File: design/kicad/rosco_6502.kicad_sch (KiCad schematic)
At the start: 54 parts, among them IC1 W65C02SxP, IC2 ATF22V10C-7PX, IC3 XR68C681CJTR-F, IC4 NE555P, IC5 ATF22V10C-7PX, J1 UART_A, J2 UART_B, J3 Conn_01x06, J4 Conn_01x01_Male, J5 Conn_02x18_Odd_Even, J6 Conn_01x02_Male, Q1 3.6864MHz, U1 AS6C4008-55PCN, U2 AS6C62256-55PCN, U3 AT28C64B-15PU, U4 74HCT174, X1 14MHz

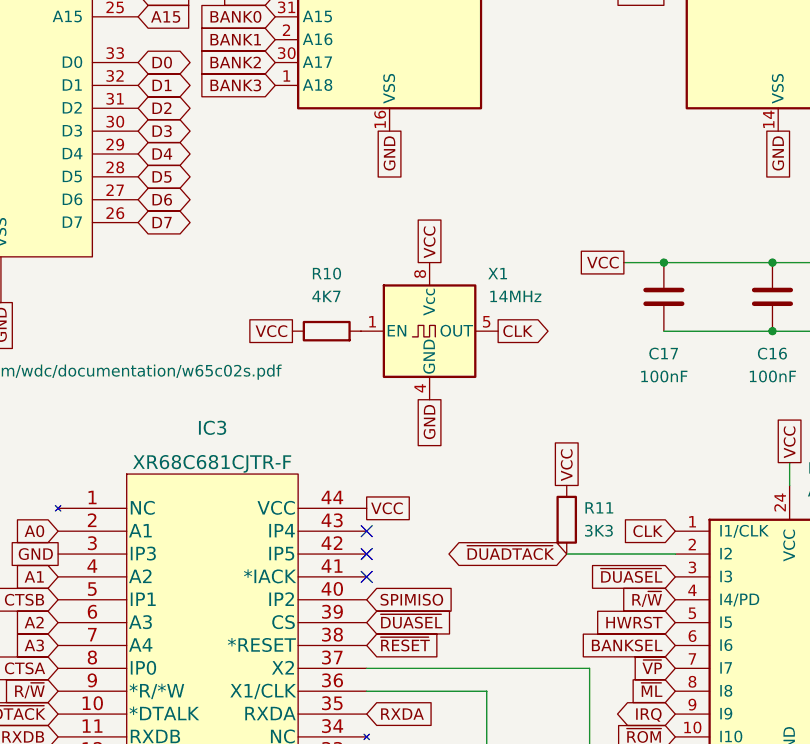
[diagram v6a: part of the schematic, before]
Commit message: Add missing DUART IACK pullup
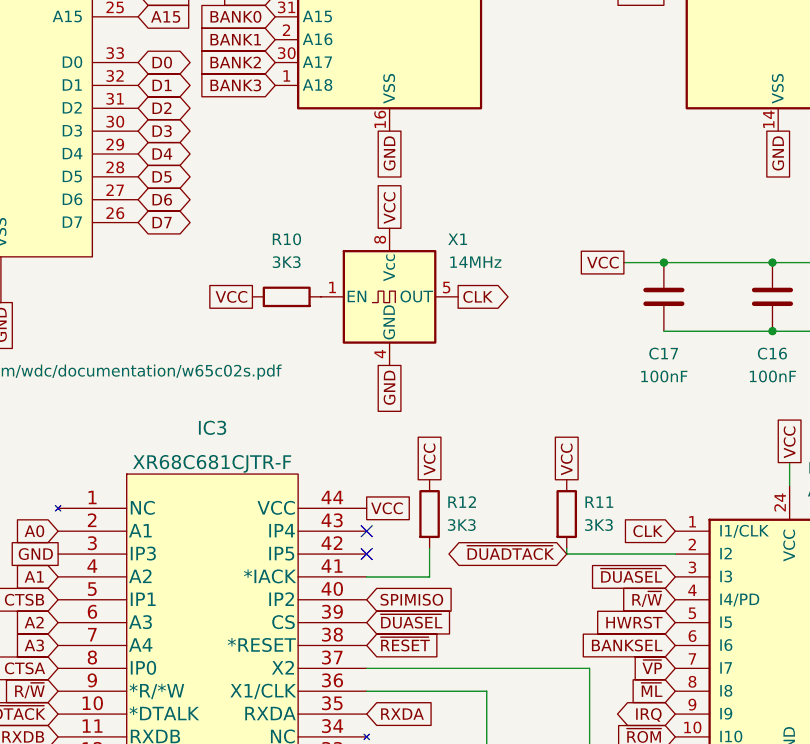
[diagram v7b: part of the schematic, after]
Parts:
- added R12: 3K3, Resistor_THT:R_Axial_DIN0207_L6.3mm_D2.5mm_P10.16mm_Horizontal, symbol Device:R
- R10: value 4K7 -> 3K3
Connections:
- net VCC: now also R12.1
- net at IC3.41 (*IACK): now also R12.2
- no-connect marks 14 -> 13
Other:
- moved on the sheet: R10, R11, X1
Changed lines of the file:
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@@
   (no_connect (at 166.37 140.335))
   (no_connect (at 166.37 135.255))
-  (no_connect (at 106.68 127.635))
   (no_connect (at 50.8 37.465))
   (no_connect (at 50.8 40.005))
+  (wire (pts (xy 113.665 124.46) (xy 113.665 127.635))
+    (stroke (width 0) (type default) (color 0 0 0 0))
+  )
   (wire (pts (xy 65.405 193.04) (xy 73.025 193.04))
     (stroke (width 0) (type default) (color 0 0 0 0))
@@
     (stroke (width 0) (type default) (color 0 0 0 0))
   )
+  (wire (pts (xy 128.905 124.46) (xy 128.905 125.095))
+    (stroke (width 0) (type default) (color 0 0 0 0))
+  )
   (wire (pts (xy 173.99 100.33) (xy 163.195 100.33))
     (stroke (width 0) (type default) (color 0 0 0 0))
@@
     (stroke (width 0) (type default) (color 0 0 0 0))
   )
+  (wire (pts (xy 113.665 127.635) (xy 106.68 127.635))
+    (stroke (width 0) (type default) (color 0 0 0 0))
+  )
   (wire (pts (xy 65.405 181.61) (xy 73.025 181.61))
     (stroke (width 0) (type default) (color 0 0 0 0))
@@
     )
   )
-  (global_label "VCC" (shape passive) (at 113.665 92.71 90) (fields_autoplaced)
+  (global_label "VCC" (shape passive) (at 109.22 88.9 90) (fields_autoplaced)
     (effects (font (size 1.27 1.27)) (justify left))
-    (property "Intersheet References" "${INTERSHEET_REFS}" (id 0) (at 113.5856 86.6683 90)
+    (property "Intersheet References" "${INTERSHEET_REFS}" (id 0) (at 109.1406 82.8583 90)
       (effects (font (size 1.27 1.27)) (justify left) hide)
     )
@@
     )
   )
-  (global_label "VCC" (shape passive) (at 98.425 100.33 180) (fields_autoplaced)
+  (global_label "VCC" (shape passive) (at 93.98 96.52 180) (fields_autoplaced)
     (effects (font (size 1.27 1.27)) (justify right))
-    (property "Intersheet References" "${INTERSHEET_REFS}" (id 0) (at 92.3833 100.4094 0)
+    (property "Intersheet References" "${INTERSHEET_REFS}" (id 0) (at 87.9383 96.5994 0)
       (effects (font (size 1.27 1.27)) (justify right) hide)
     )
@@
     )
   )
-  (global_label "CLK" (shape output) (at 121.285 100.33 0) (fields_autoplaced)
+  (global_label "CLK" (shape output) (at 116.84 96.52 0) (fields_autoplaced)
     (effects (font (size 1.27 1.27)) (justify left))
-    (property "Intersheet References" "${INTERSHEET_REFS}" (id 0) (at 127.2662 100.2506 0)
+    (property "Intersheet References" "${INTERSHEET_REFS}" (id 0) (at 122.8212 96.4406 0)
       (effects (font (size 1.27 1.27)) (justify left) hide)
     )
@@
     )
   )
-  (global_label "GND" (shape passive) (at 113.665 107.95 270) (fields_autoplaced)
+  (global_label "GND" (shape passive) (at 109.22 104.14 270) (fields_autoplaced)
     (effects (font (size 1.27 1.27)) (justify right))
-    (property "Intersheet References" "${INTERSHEET_REFS}" (id 0) (at 113.5856 114.2336 90)
+    (property "Intersheet References" "${INTERSHEET_REFS}" (id 0) (at 109.1406 110.4236 90)
       (effects (font (size 1.27 1.27)) (justify right) hide)
     )
@@
     )
   )
+  (global_label "VCC" (shape passive) (at 113.665 116.84 90) (fields_autoplaced)
+    (effects (font (size 1.27 1.27)) (justify left))
+    (property "Intersheet References" "${INTERSHEET_REFS}" (id 0) (at 113.5856 110.7983 90)
+      (effects (font (size 1.27 1.27)) (justify left) hide)
+    )
+  )
   (global_label "A0" (shape input) (at 182.245 27.305 180) (fields_autoplaced)
     (effects (font (size 1.27 1.27)) (justify right))
@@
     )
   )
-  (global_label "VCC" (shape passive) (at 128.905 117.475 90) (fields_autoplaced)
+  (global_label "VCC" (shape passive) (at 128.905 116.84 90) (fields_autoplaced)
     (effects (font (size 1.27 1.27)) (justify left))
-    (property "Intersheet References" "${INTERSHEET_REFS}" (id 0) (at 128.8256 111.4333 90)
+    (property "Intersheet References" "${INTERSHEET_REFS}" (id 0) (at 128.8256 110.7983 90)
       (effects (font (size 1.27 1.27)) (justify left) hide)
     )
@@
     (pin "2")
   )
-  (symbol (lib_id "Oscillator:CXO_DIP8") (at 113.665 100.33 0) (unit 1)
+  (symbol (lib_id "Oscillator:CXO_DIP8") (at 109.22 96.52 0) (unit 1)
     (in_bom yes) (on_board yes)
-    (property "Reference" "X1" (id 0) (at 121.285 93.98 0))
-    (property "Value" "14MHz" (id 1) (at 123.19 96.52 0))
-    (property "Footprint" "Oscillator:Oscillator_DIP-8" (id 2) (at 125.095 109.22 0)
+    (property "Reference" "X1" (id 0) (at 116.84 90.17 0))
+    (property "Value" "14MHz" (id 1) (at 118.745 92.71 0))
+    (property "Footprint" "Oscillator:Oscillator_DIP-8" (id 2) (at 120.65 105.41 0)
       (effects (font (size 1.27 1.27)) hide)
     )
-    (property "Datasheet" "http://cdn-reichelt.de/documents/datenblatt/B400/OSZI.pdf" (id 3) (at 111.125 100.33 0)
+    (property "Datasheet" "http://cdn-reichelt.de/documents/datenblatt/B400/OSZI.pdf" (id 3) (at 106.68 96.52 0)
       (effects (font (size 1.27 1.27)) hide)
     )
@@
     (pin "9")
   )
-  (symbol (lib_id "Device:R") (at 102.235 100.33 90) (unit 1)
+  (symbol (lib_id "Device:R") (at 97.79 96.52 90) (unit 1)
     (in_bom yes) (on_board yes) (fields_autoplaced)
-    (property "Reference" "R10" (id 0) (at 102.235 93.98 90))
-    (property "Value" "4K7" (id 1) (at 102.235 96.52 90))
-    (property "Footprint" "Resistor_THT:R_Axial_DIN0207_L6.3mm_D2.5mm_P10.16mm_Horizontal" (id 2) (at 102.235 102.108 90)
+    (property "Reference" "R10" (id 0) (at 97.79 90.17 90))
+    (property "Value" "3K3" (id 1) (at 97.79 92.71 90))
+    (property "Footprint" "Resistor_THT:R_Axial_DIN0207_L6.3mm_D2.5mm_P10.16mm_Horizontal" (id 2) (at 97.79 98.298 90)
       (effects (font (size 1.27 1.27)) hide)
     )
-    (property "Datasheet" "~" (id 3) (at 102.235 100.33 0)
+    (property "Datasheet" "~" (id 3) (at 97.79 96.52 0)
       (effects (font (size 1.27 1.27)) hide)
     )
@@
     (pin "2")
   )
+  (symbol (lib_id "Device:R") (at 113.665 120.65 0) (unit 1)
+    (in_bom yes) (on_board yes) (fields_autoplaced)
+    (property "Reference" "R12" (id 0) (at 115.57 119.3799 0)
+      (effects (font (size 1.27 1.27)) (justify left))
+    )
+    (property "Value" "3K3" (id 1) (at 115.57 121.9199 0)
+      (effects (font (size 1.27 1.27)) (justify left))
+    )
+    (property "Footprint" "Resistor_THT:R_Axial_DIN0207_L6.3mm_D2.5mm_P10.16mm_Horizontal" (id 2) (at 111.887 120.65 90)
+      (effects (font (size 1.27 1.27)) hide)
+    )
+    (property "Datasheet" "~" (id 3) (at 113.665 120.65 0)
+      (effects (font (size 1.27 1.27)) hide)
+    )
+    (pin "1")
+    (pin "2")
+  )
   (symbol (lib_id "rosco_6502:GAL22V10") (at 255.905 132.715 0) (unit 1)
     (in_bom yes) (on_board yes) (fields_autoplaced)
@@
     (pin "2")
   )
-  (symbol (lib_id "Device:R") (at 128.905 121.285 0) (unit 1)
+  (symbol (lib_id "Device:R") (at 128.905 120.65 0) (unit 1)
     (in_bom yes) (on_board yes) (fields_autoplaced)
-    (property "Reference" "R11" (id 0) (at 130.81 120.0149 0)
+    (property "Reference" "R11" (id 0) (at 130.81 119.3799 0)
       (effects (font (size 1.27 1.27)) (justify left))
     )
-    (property "Value" "3K3" (id 1) (at 130.81 122.5549 0)
+    (property "Value" "3K3" (id 1) (at 130.81 121.9199 0)
       (effects (font (size 1.27 1.27)) (justify left))
     )
-    (property "Footprint" "Resistor_THT:R_Axial_DIN0207_L6.3mm_D2.5mm_P10.16mm_Horizontal" (id 2) (at 127.127 121.285 90)
+    (property "Footprint" "Resistor_THT:R_Axial_DIN0207_L6.3mm_D2.5mm_P10.16mm_Horizontal" (id 2) (at 127.127 120.65 90)
       (effects (font (size 1.27 1.27)) hide)
     )
-    (property "Datasheet" "~" (id 3) (at 128.905 121.285 0)
+    (property "Datasheet" "~" (id 3) (at 128.905 120.65 0)
       (effects (font (size 1.27 1.27)) hide)
     )
@@
     )
     (path "/88884666-6a7a-4147-9f62-1b097673c5ca"
-      (reference "R10") (unit 1) (value "4K7") (footprint "Resistor_THT:R_Axial_DIN0207_L6.3mm_D2.5mm_P10.16mm_Horizontal")
+      (reference "R10") (unit 1) (value "3K3") (footprint "Resistor_THT:R_Axial_DIN0207_L6.3mm_D2.5mm_P10.16mm_Horizontal")
     )
     (path "/f5dcec41-5ab5-44ff-9edb-8c415c1256fa"
       (reference "R11") (unit 1) (value "3K3") (footprint "Resistor_THT:R_Axial_DIN0207_L6.3mm_D2.5mm_P10.16mm_Horizontal")
     )
+    (path "/99fd5e96-224d-4164-93ab-fbf3163b223f"
+      (reference "R12") (unit 1) (value "3K3") (footprint "Resistor_THT:R_Axial_DIN0207_L6.3mm_D2.5mm_P10.16mm_Horizontal")
+    )
     (path "/8a9d55c4-cad3-46c0-840f-2a6683619b87"

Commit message: r3
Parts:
- added J7: Jack-DC, Connector_BarrelJack:BarrelJack_Horizontal, symbol Connector:Jack-DC
- renumbered C10 to C1, C17 to C10, C12 to C11, C2 to C12, C6 to C13, C7 to C14, C13 to C15, C3 to C16, C5 to C17, C4 to C18, C9 to C19, C11 to C2, C8 to C20, C1 to C3, C14 to C4, C16 to C8, C15 to C9
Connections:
- net GND: now also J7.2
- net VCC: now also J7.1
